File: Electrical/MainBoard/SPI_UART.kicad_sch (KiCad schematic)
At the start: 2 parts, among them J2 UART Connect, J3 SPI Connect

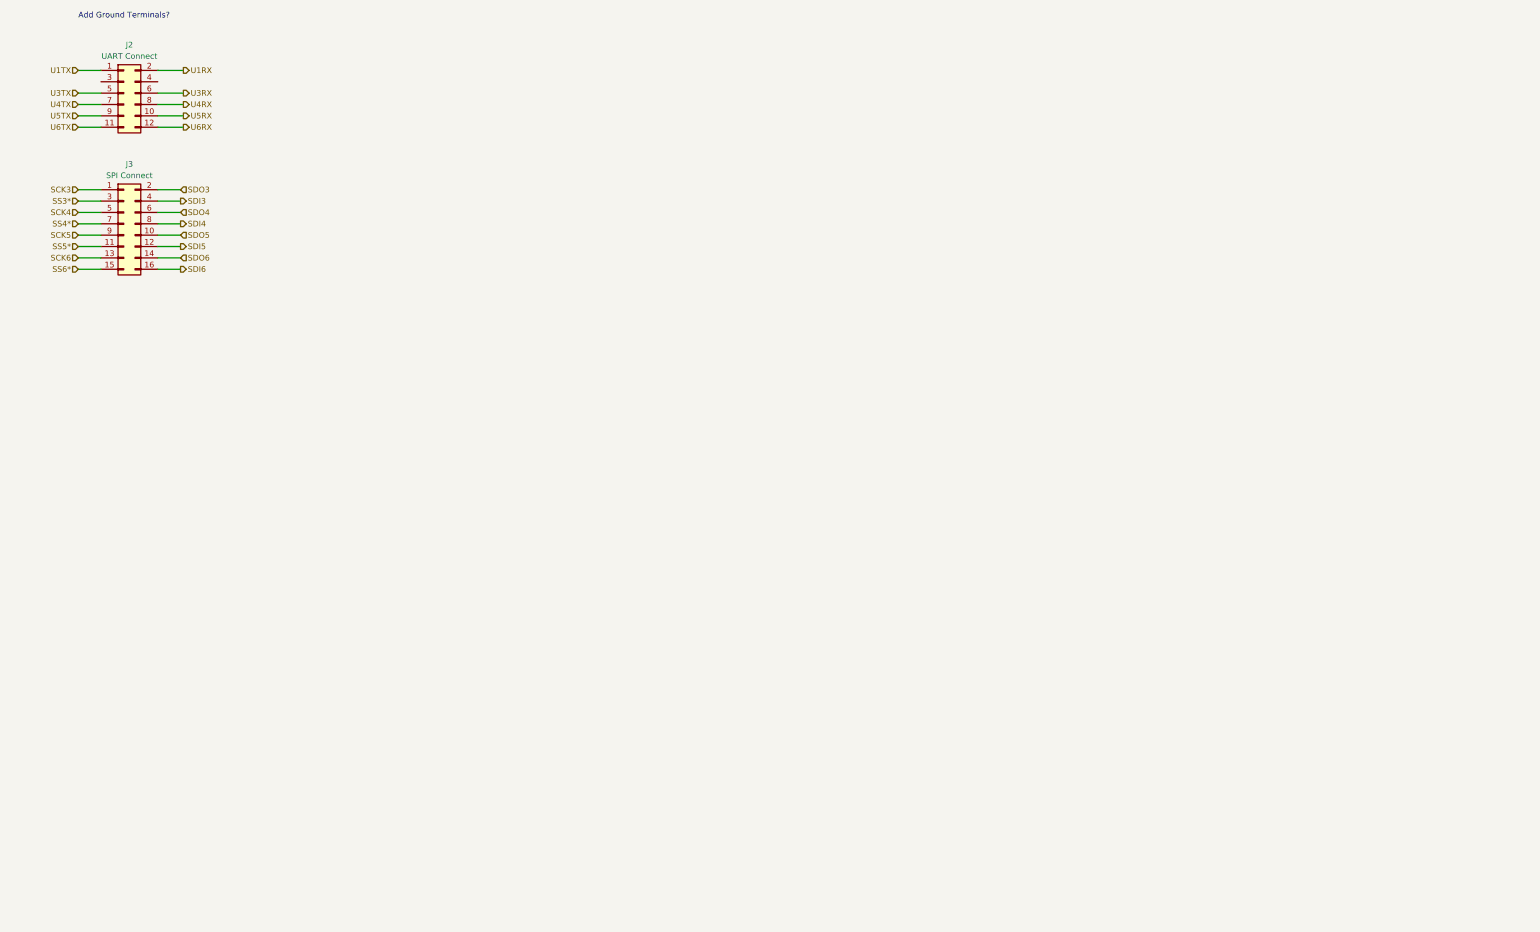
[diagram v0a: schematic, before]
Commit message: Add more schematics and begin floorplanning
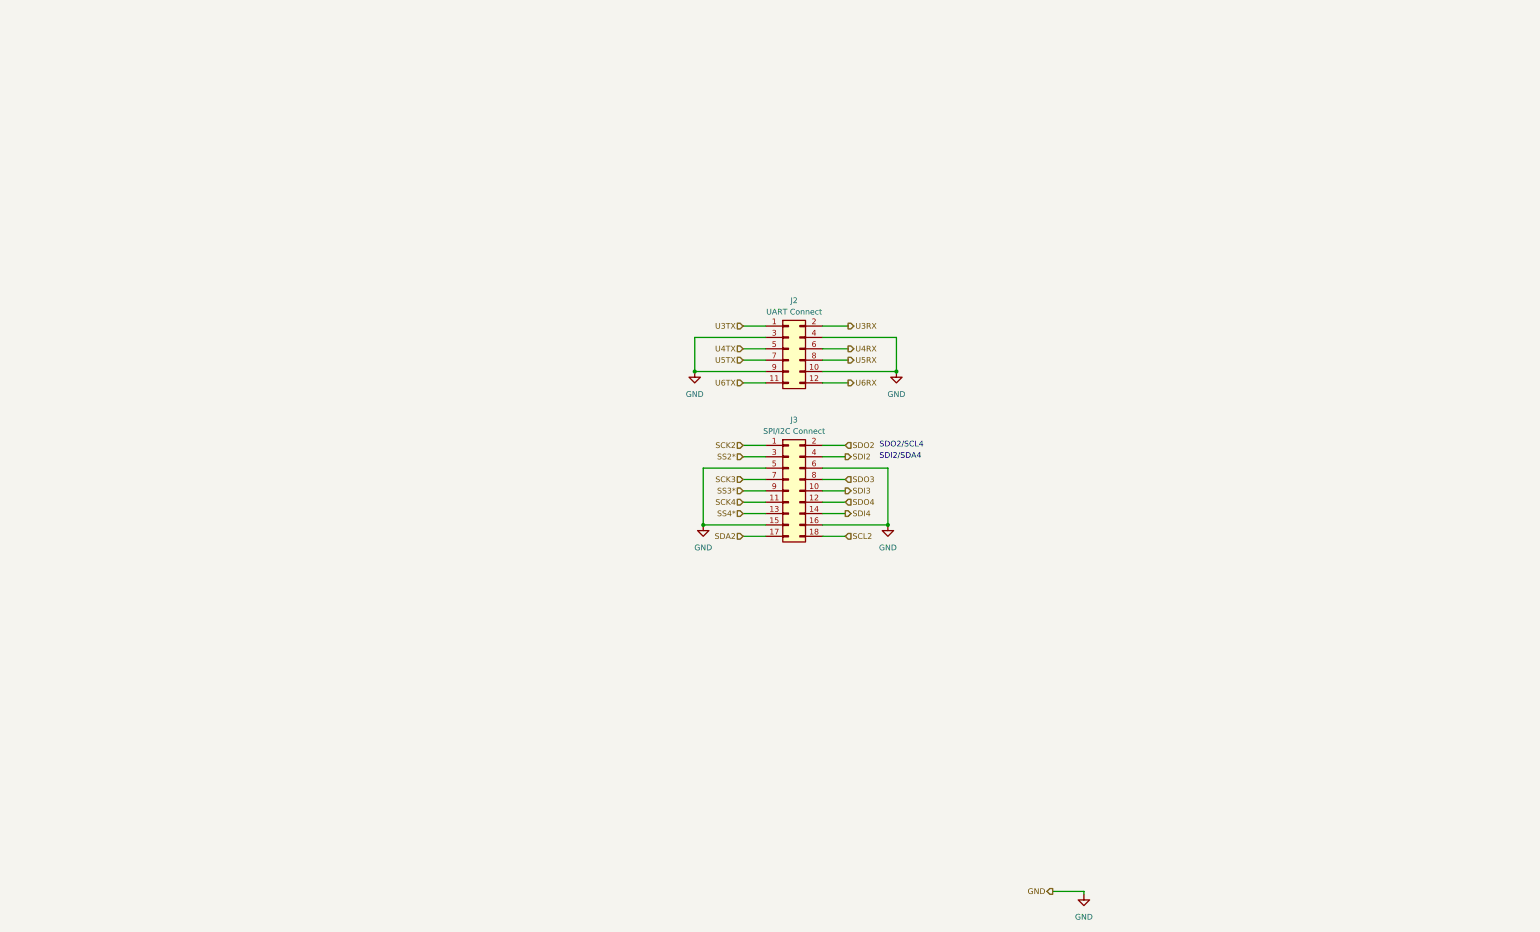
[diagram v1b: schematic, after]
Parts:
- removed J3: SPI Connect, Connector_PinHeader_2.54mm:PinHeader_2x08_P2.54mm_Vertical, symbol Connector_Generic:Conn_02x08_Odd_Even
- added J3: SPI/I2C Connect, Connector_PinHeader_2.54mm:PinHeader_2x09_P2.54mm_Vertical, symbol Connector_Generic:Conn_02x09_Odd_Even
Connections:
- net U1RX is gone; now on net U3RX: J2.2 (Pin_2)
- net U1TX is gone; now on net U3TX: J2.1 (Pin_1)
- net SCK3: now also J3.7 (Pin_7)
- net SCK4: now also J3.11 (Pin_11)
- net SDI3: now also J3.10 (Pin_10)
- net SDI4: now also J3.14 (Pin_14)
- net SDO3: now also J3.8 (Pin_8)
- net SDO4: now also J3.12 (Pin_12)
- net SS3*: now also J3.9 (Pin_9)
- net SS4*: now also J3.13 (Pin_13)
- net U3RX: no longer J2.6 (Pin_6)
- net U3TX: no longer J2.5 (Pin_5)
- net U4RX: now also J2.6 (Pin_6); no longer J2.8 (Pin_8)
- net U4TX: now also J2.5 (Pin_5); no longer J2.7 (Pin_7)
- net U5RX: now also J2.8 (Pin_8); no longer J2.10 (Pin_10)
- net U5TX: now also J2.7 (Pin_7); no longer J2.9 (Pin_9)
- net GND: now reaches J2.3 (Pin_3)
- net GND: now also J2.10 (Pin_10), J2.4 (Pin_4), J2.9 (Pin_9), J3.15 (Pin_15), J3.16 (Pin_16), J3.5 (Pin_5), J3.6 (Pin_6)
- new net SCK2: J3.1 (Pin_1)
- new net SCL2: J3.18 (Pin_18)
- new net SDA2: J3.17 (Pin_17)
- new net SDI2: J3.4 (Pin_4)
- new net SDO2: J3.2 (Pin_2)
- new net SS2*: J3.3 (Pin_3)
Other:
- note added: "SDI2/SDA4"
- note added: "SDO2/SCL4"
- note removed: "Add Ground Terminals?"
- moved on the sheet: J2

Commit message: Begin layout of pcb
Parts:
- renumbered J2 to J7, J3 to J8
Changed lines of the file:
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@@
         )
         (path "/bd24c4db-4e36-4117-bd4f-5228ef241da9/d895d168-5c3b-4f65-b0f2-4d47b39f1a08"
-          (reference "#PWR0112") (unit 1)
+          (reference "#PWR082") (unit 1)
         )
       )
@@
         )
         (path "/bd24c4db-4e36-4117-bd4f-5228ef241da9/d895d168-5c3b-4f65-b0f2-4d47b39f1a08"
-          (reference "#PWR0116") (unit 1)
+          (reference "#PWR078") (unit 1)
         )
       )
@@
         )
         (path "/bd24c4db-4e36-4117-bd4f-5228ef241da9/d895d168-5c3b-4f65-b0f2-4d47b39f1a08"
-          (reference "#PWR0118") (unit 1)
+          (reference "#PWR080") (unit 1)
         )
       )
@@
         )
         (path "/bd24c4db-4e36-4117-bd4f-5228ef241da9/d895d168-5c3b-4f65-b0f2-4d47b39f1a08"
-          (reference "#PWR0119") (unit 1)
+          (reference "#PWR079") (unit 1)
         )
       )
@@
   (symbol (lib_id "Connector_Generic:Conn_02x09_Odd_Even") (at 229.235 158.115 0) (unit 1)
     (in_bom yes) (on_board yes) (dnp no) (fields_autoplaced)
-    (property "Reference" "J3" (at 230.505 142.24 0)
+    (property "Reference" "J8" (at 230.505 142.24 0)
       (effects (font (size 1.27 1.27)))
     )
@@
       (project "MainBoard"
         (path "/bd24c4db-4e36-4117-bd4f-5228ef241da9/d895d168-5c3b-4f65-b0f2-4d47b39f1a08"
-          (reference "J3") (unit 1)
+          (reference "J8") (unit 1)
         )
       )
@@
   (symbol (lib_id "Connector_Generic:Conn_02x06_Odd_Even") (at 229.235 126.365 0) (unit 1)
     (in_bom yes) (on_board yes) (dnp no) (fields_autoplaced)
-    (property "Reference" "J2" (at 230.505 115.57 0)
+    (property "Reference" "J7" (at 230.505 115.57 0)
       (effects (font (size 1.27 1.27)))
     )
@@
       (project "MainBoard"
         (path "/bd24c4db-4e36-4117-bd4f-5228ef241da9/d895d168-5c3b-4f65-b0f2-4d47b39f1a08"
-          (reference "J2") (unit 1)
+          (reference "J7") (unit 1)
         )
       )
@@
         )
         (path "/bd24c4db-4e36-4117-bd4f-5228ef241da9/d895d168-5c3b-4f65-b0f2-4d47b39f1a08"
-          (reference "#PWR0115") (unit 1)
-        )
-      )
+          (reference "#PWR081") (unit 1)
+        )
+      )

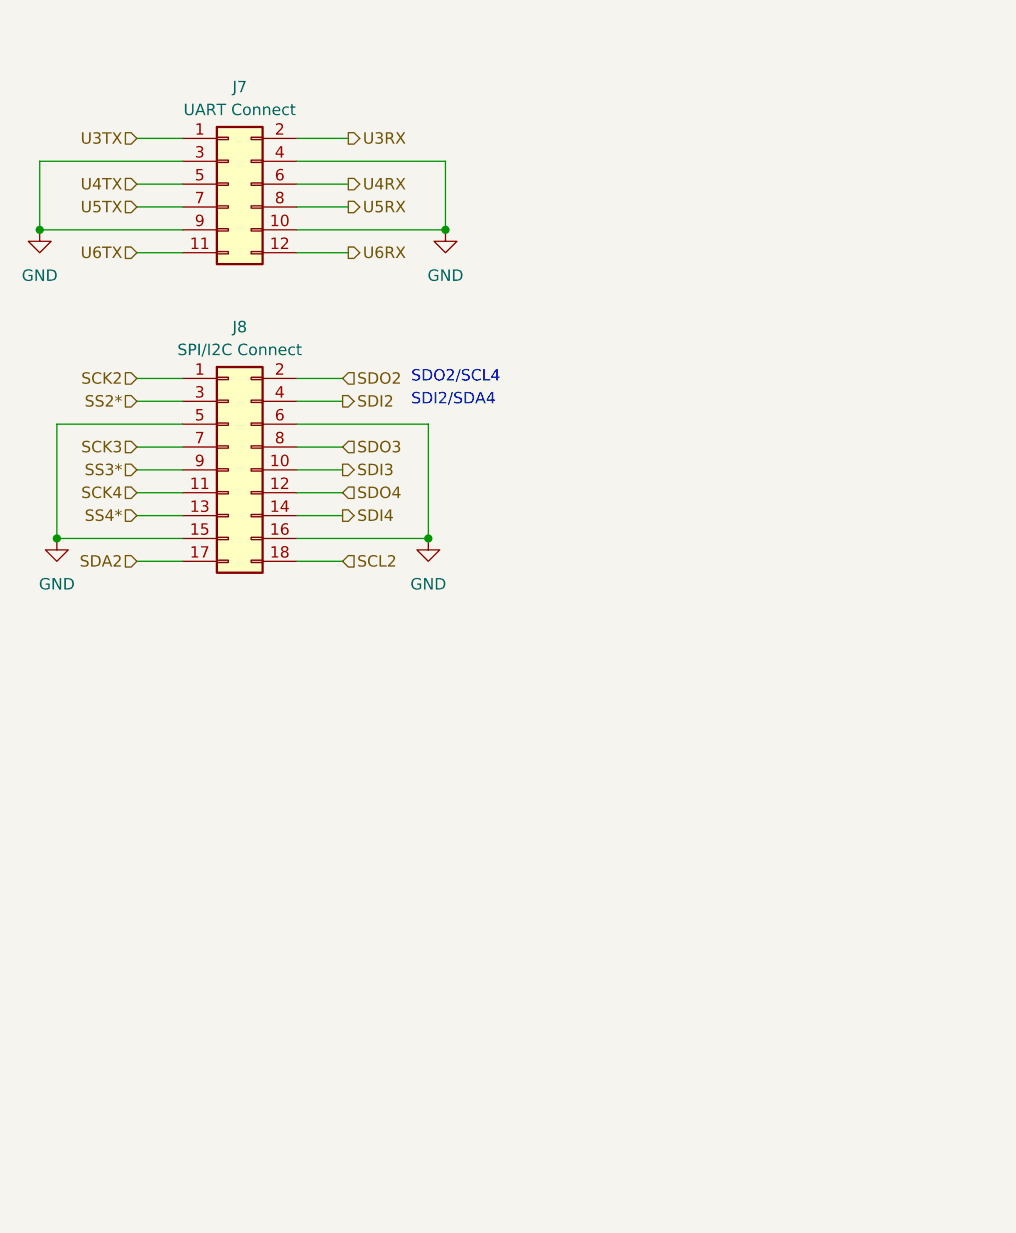
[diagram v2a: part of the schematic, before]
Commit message: First Pass at the routing
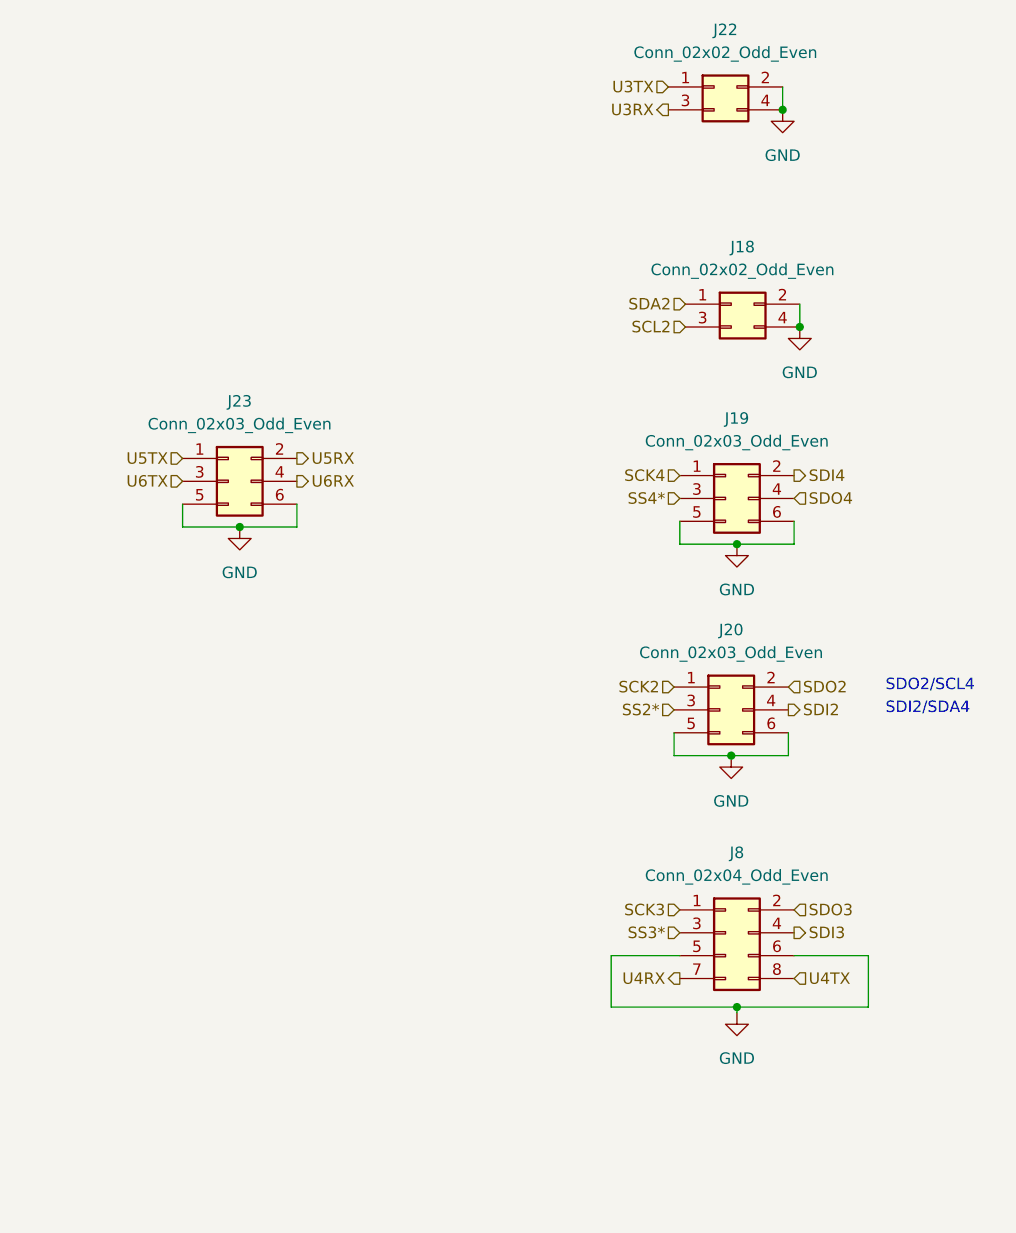
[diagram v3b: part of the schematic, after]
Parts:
- removed J7: UART Connect, Connector_PinHeader_2.54mm:PinHeader_2x06_P2.54mm_Vertical, symbol Connector_Generic:Conn_02x06_Odd_Even
- removed J8: SPI/I2C Connect, Connector_PinHeader_2.54mm:PinHeader_2x09_P2.54mm_Vertical, symbol Connector_Generic:Conn_02x09_Odd_Even
- added J18, J22: Conn_02x02_Odd_Even, Connector_PinHeader_2.54mm:PinHeader_2x02_P2.54mm_Vertical, symbol Connector_Generic:Conn_02x02_Odd_Even
- added J19, J20, J23: Conn_02x03_Odd_Even, Connector_PinHeader_2.54mm:PinHeader_2x03_P2.54mm_Vertical, symbol Connector_Generic:Conn_02x03_Odd_Even
- added J8: Conn_02x04_Odd_Even, Connector_PinHeader_2.54mm:PinHeader_2x04_P2.54mm_Vertical, symbol Connector_Generic:Conn_02x04_Odd_Even
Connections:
- net GND: now also J18.2 (Pin_2), J18.4 (Pin_4), J19.5 (Pin_5), J19.6 (Pin_6), J20.5 (Pin_5), J20.6 (Pin_6), J22.2 (Pin_2), J22.4 (Pin_4), J23.5 (Pin_5), J23.6 (Pin_6), J8.5 (Pin_5), J8.6 (Pin_6)
- net SCK2: now also J20.1 (Pin_1)
- net SCK3: now also J8.1 (Pin_1)
- net SCK4: now also J19.1 (Pin_1)
- net SCL2: now also J18.3 (Pin_3)
- net SDA2: now also J18.1 (Pin_1)
- net SDI2: now also J20.4 (Pin_4)
- net SDI3: now also J8.4 (Pin_4)
- net SDI4: now also J19.2 (Pin_2)
- net SDO2: now also J20.2 (Pin_2)
- net SDO3: now also J8.2 (Pin_2)
- net SDO4: now also J19.4 (Pin_4)
- net SS2*: now also J20.3 (Pin_3)
- net SS3*: now also J8.3 (Pin_3)
- net SS4*: now also J19.3 (Pin_3)
- net U3RX: now also J22.3 (Pin_3)
- net U3TX: now also J22.1 (Pin_1)
- net U4RX: now also J8.7 (Pin_7)
- net U4TX: now also J8.8 (Pin_8)
- net U5RX: now also J23.2 (Pin_2)
- net U5TX: now also J23.1 (Pin_1)
- net U6RX: now also J23.4 (Pin_4)
- net U6TX: now also J23.3 (Pin_3)

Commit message: Add some finishing touches and create preliminary boms
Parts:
- J18, J22: Mfr (none) -> Amphenol ICC (FCI); Mfr P/N (none) -> 10129381-904003BLF; Supplier 1 (none) -> DigiKey; Supplier 1 P/N (none) -> 10129381-904003BLF-ND
- J19, J20, J23: Mfr (none) -> Amphenol ICC (FCI); Mfr P/N (none) -> 10129381-906002BLF; Supplier 1 (none) -> DigiKey; Supplier 1 P/N (none) -> 10129381-906002BLF-ND
- J8: Mfr (none) -> Amphenol ICC (FCI); Mfr P/N (none) -> 10129381-908001BLF; Supplier 1 (none) -> DigiKey; Supplier 1 P/N (none) -> 10129381-908001BLF-ND

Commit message: Made V0.2 revisions to Main Board
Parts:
- removed J20: Conn_02x03_Odd_Even, Connector_PinHeader_2.54mm:PinHeader_2x03_P2.54mm_Vertical, symbol Connector_Generic:Conn_02x03_Odd_Even
- added J20: Conn_01x06, Connector_Molex:Molex_KK-254_AE-6410-06A_1x06_P2.54mm_Vertical, symbol Connector_Generic:Conn_01x06
- added J27: Conn_01x06_Socket, symbol Connector:Conn_01x06_Socket
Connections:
- net GND: now also J20.5 (Pin_5), J20.6 (Pin_6)
- net SCK2: now also J20.1 (Pin_1)
- net SDI2: now also J20.4 (Pin_4)
- net SDO2: now also J20.3 (Pin_3)
- net SS2*: now also J20.2 (Pin_2)
- no-connect marks 0 -> 6
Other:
- note added: "Pairs with DigiKey PN WM2015-ND"
- note added: "Primary use is for Jetson"
